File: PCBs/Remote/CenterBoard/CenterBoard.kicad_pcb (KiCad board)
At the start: 4 copper layers, 100 x 100 mm, 83 parts, among them J201 DX07S016JA1R1500, J401 SMA, J501 Conn_01x11, J701 Conn_02x10_Odd_Even, U201 LPC51U68JBD64, U202 W25Q128JVS, U301 SC189ZSKTRT, U401 nRF24L01P, U402 RFX2401C, U601 Joystick Left, U602 Joystick Right, U701 74HC14, U702 74HC14, U703 74HC14, X401 16MHz

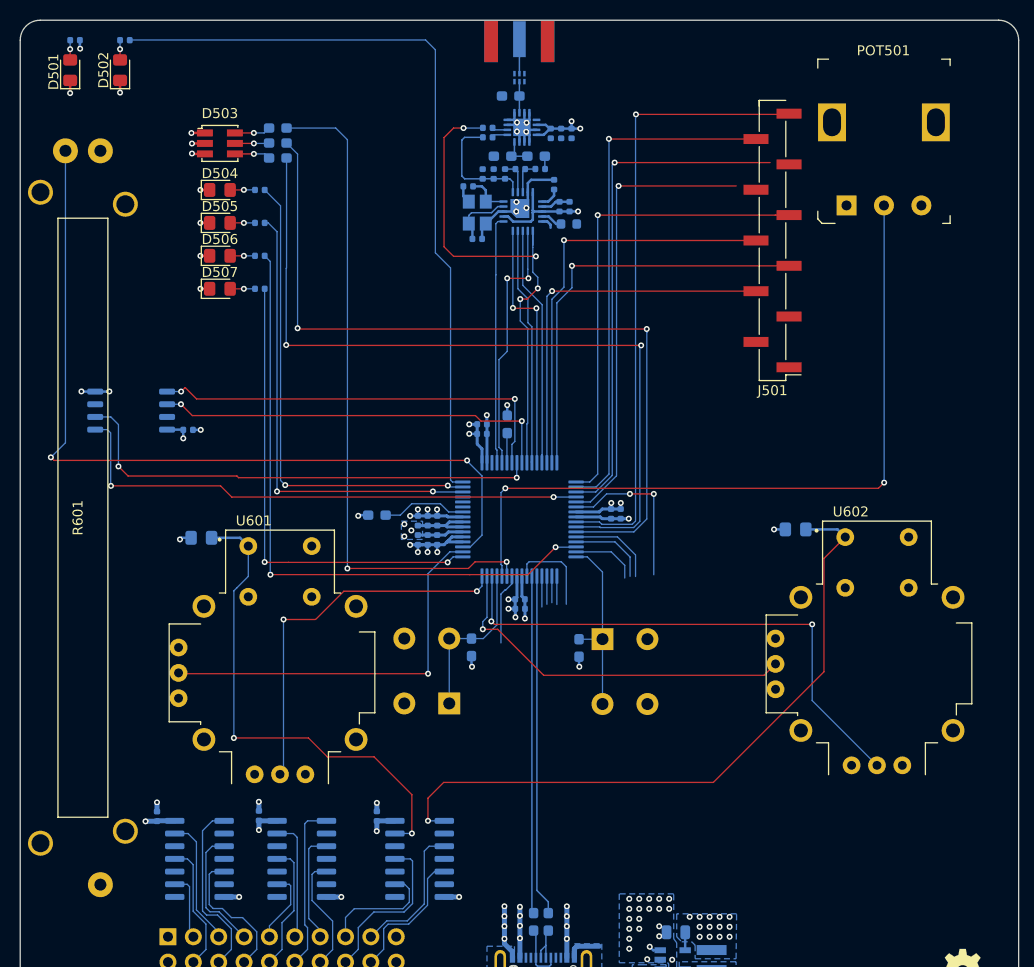
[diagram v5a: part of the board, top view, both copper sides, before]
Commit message: Finished leds, redid a lot of PCB wiring. Almost done there now.
Signed-off-by: Eldalote.Electronics <Eldalote.Electronics@gmail.com>
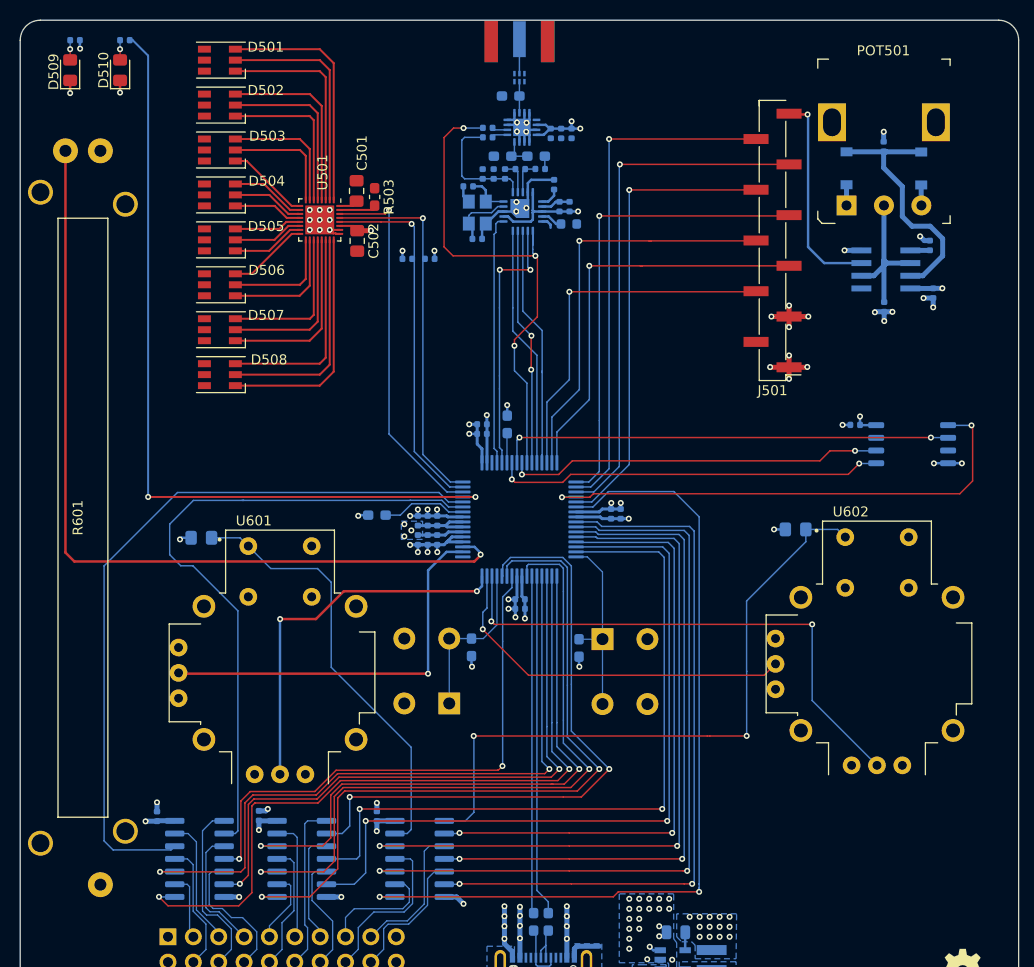
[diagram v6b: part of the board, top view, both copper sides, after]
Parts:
- removed R507, R508, R509: 560R, Resistor_SMD:R_0402_1005Metric
- added C501: 1uF, Capacitor_SMD:C_0805_2012Metric_Pad1.15x1.40mm_HandSolder, F.Cu at (133.7, 77.1)
- added C502: 100nF, Capacitor_SMD:C_0805_2012Metric_Pad1.15x1.40mm_HandSolder, F.Cu at (133.8, 82.1)
- added C503: 100nF, Capacitor_SMD:C_0402_1005Metric, B.Cu at (186.5, 88.7)
- added C504: 100nF, Capacitor_SMD:C_0402_1005Metric, B.Cu at (191.1, 82.6)
- added C505: 100nF, Capacitor_SMD:C_0402_1005Metric, B.Cu at (191.4, 87.3)
- added D501: User LED RGB 0, LED_SMD:LED_RGB_PLCC-6, F.Cu at (120.0, 64.0)
- added D502: User LED RGB 1, LED_SMD:LED_RGB_PLCC-6, F.Cu at (120.0, 68.5)
- added D508: User LED RGB 7, LED_SMD:LED_RGB_PLCC-6, F.Cu at (120.0, 95.5)
- added D511: BAT54GWJ, Diode_SMD:D_SOD-123, B.Cu at (190.2, 74.8)
- added D512: BAT54GWJ, Diode_SMD:D_SOD-123, B.Cu at (182.8, 74.8)
- added U501: LP5024, Package_DFN_QFN:QFN-32-1EP_4x4mm_P0.4mm_EP2.9x2.9mm, F.Cu at (130.0, 80.0)
- added U502: TLC555CDR, digikey-footprints:SOIC-8_W3.9mm, B.Cu at (186.7, 85.0)
- D503: value RGB User LED -> User LED RGB 2; footprint digikey-footprints:6-PLCC_3.5x3.5mm -> LED_SMD:LED_RGB_PLCC-6
- D504: value LED_USER_0 -> User LED RGB 3; footprint LED_SMD:LED_0805_2012Metric_Pad1.15x1.40mm_HandSolder -> LED_SMD:LED_RGB_PLCC-6
- D505: value LED_USER_1 -> User LED RGB 4; footprint LED_SMD:LED_0805_2012Metric_Pad1.15x1.40mm_HandSolder -> LED_SMD:LED_RGB_PLCC-6
- D506: value LED_USER_2 -> User LED RGB 5; footprint LED_SMD:LED_0805_2012Metric_Pad1.15x1.40mm_HandSolder -> LED_SMD:LED_RGB_PLCC-6
- D507: value LED_USER_3 -> User LED RGB 6; footprint LED_SMD:LED_0805_2012Metric_Pad1.15x1.40mm_HandSolder -> LED_SMD:LED_RGB_PLCC-6
- POT501: value Screen brightness Potentiometer -> P120PKY25BR10K
- R503: value 30R -> 7k32; moved to F.Cu
- R504: value 240R -> 1k; footprint Resistor_SMD:R_0603_1608Metric_Pad1.05x0.95mm_HandSolder -> Resistor_SMD:R_0402_1005Metric
- R505: value 240R -> 4k7; footprint Resistor_SMD:R_0603_1608Metric_Pad1.05x0.95mm_HandSolder -> Resistor_SMD:R_0402_1005Metric
- R506: value 560R -> 4k7
- moved U202 78.3 mm to (189.3, 102.5), turned to 180 degrees
- moved C214 66.8 mm to (183.6, 100.5), turned to 180 degrees
- moved R504 60.7 mm to (186.5, 72.7), turned to 90 degrees
- moved R506 18.4 mm to (141.0, 83.9)
- moved R505 16.4 mm to (138.8, 83.9)
- moved R503 11.9 mm to (135.5, 77.7), turned to 270 degrees
- moved D507 4.10 mm to (120.0, 91.0), turned to 180 degrees
- moved D506 2.90 mm to (120.0, 86.5), turned to 180 degrees
- moved D505 1.70 mm to (120.0, 82.0), turned to 180 degrees
- moved D503 0.66 mm to (120.0, 73.0), turned to 180 degrees
- moved D504 0.50 mm to (120.0, 77.5), turned to 180 degrees
- renumbered D501 to D509, D502 to D510
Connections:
- D503 pad 1: GND -> Net-(D503-Pad1)
- D503 pad 2: GND -> Net-(D503-Pad2)
- D503 pad 3: GND -> Net-(D503-Pad3)
- D503 pad 4: Net-(D503-Pad4) -> +3V3
- D503 pad 5: Net-(D503-Pad5) -> +3V3
- D503 pad 6: Net-(D503-Pad6) -> +3V3
- D504 pad 1: GND -> Net-(D504-Pad1)
- D505 pad 1: GND -> Net-(D505-Pad1)
- D506 pad 1: GND -> Net-(D506-Pad1)
- D507 pad 1: GND -> Net-(D507-Pad1)
- J501 pad 11: Screen_Backlight_PWM -> /LEDs and Screen/Backlight_PWM
- POT501 pad 1: GND -> Net-(D512-Pad1)
- POT501 pad 2: Screen_Backlight_pot -> /LEDs and Screen/TRIG
- POT501 pad 3: +3V3 -> Net-(D511-Pad2)
- R503 pad 1: LED_USER_RGB_B -> GND
- R503 pad 2: Net-(D503-Pad6) -> Net-(R503-Pad2)
- R504 pad 1: LED_USER_RGB_G -> /LEDs and Screen/DISCH
- R504 pad 2: Net-(D503-Pad5) -> +3V3
- R505 pad 1: LED_USER_RGB_R -> LED_RGB_I2C_SDA
- R505 pad 2: Net-(D503-Pad4) -> +3V3
- R506 pad 1: Net-(D504-Pad2) -> LED_RGB_I2C_SCL
- R506 pad 2: USER_LED_0 -> +3V3
- U201 pad 1: Net-(U201-Pad1) -> KB_SW_6
- U201 pad 10: Net-(U201-Pad10) -> KB_SW_5
- U201 pad 11: LED_USER_RGB_B -> KB_SW_point
- U201 pad 12: Screen_Backlight_pot -> KB_SW_9
- U201 pad 17: USER_LED_3 -> Net-(U201-Pad17)
- U201 pad 2: Net-(U201-Pad2) -> KB_SW_7
- U201 pad 27: Net-(U201-Pad27) -> KB_SW_0
- U201 pad 28: Net-(U201-Pad28) -> KB_SW_1
- U201 pad 29: Net-(U201-Pad29) -> LED_ERROR
- U201 pad 3: Net-(U201-Pad3) -> KB_SW_8
- U201 pad 30: USER_LED_1 -> LED_RGB_EN
- U201 pad 31: USER_LED_0 -> LED_RGB_I2C_SDA
- U201 pad 32: LED_ERROR -> LED_RGB_I2C_SCL
- U201 pad 4: Net-(U201-Pad4) -> KB_SW_4
- U201 pad 51: Net-(U201-Pad51) -> Screen_TFT_DC
- U201 pad 53: Net-(U201-Pad53) -> Screen_TFT_RESET
- U201 pad 54: Net-(U201-Pad54) -> KB_SW_M3
- U201 pad 57: Screen_Backlight_PWM -> KB_SW_M1
- U201 pad 58: LED_USER_RGB_R -> KB_SW_M0
- U201 pad 59: LED_USER_RGB_G -> KB_SW_M2
- U201 pad 60: Net-(U201-Pad60) -> JS_left_button_out
- U201 pad 61: Net-(U201-Pad61) -> JS_right_button_out
- U201 pad 62: USER_LED_2 -> KB_SW_3
- U201 pad 63: Net-(U201-Pad63) -> KB_SW_ENTER
- U201 pad 7: Net-(U201-Pad7) -> KB_SW_2
- U701 pad 10: Net-(U701-Pad10) -> KB_SW_4
- U701 pad 12: Net-(U701-Pad12) -> KB_SW_1
- U701 pad 2: Net-(U701-Pad2) -> KB_SW_0
- U701 pad 4: Net-(U701-Pad4) -> KB_SW_5
- U701 pad 6: Net-(U701-Pad6) -> KB_SW_8
- U701 pad 8: Net-(U701-Pad8) -> KB_SW_7
- U702 pad 10: Net-(U702-Pad10) -> KB_SW_2
- U702 pad 12: Net-(U702-Pad12) -> KB_SW_6
- U702 pad 2: Net-(U702-Pad2) -> KB_SW_9
- U702 pad 4: Net-(U702-Pad4) -> KB_SW_ENTER
- U702 pad 6: Net-(U702-Pad6) -> KB_SW_3
- U702 pad 8: Net-(U702-Pad8) -> KB_SW_point
- U703 pad 10: Net-(U703-Pad10) -> KB_SW_M0
- U703 pad 12: Net-(U703-Pad12) -> JS_left_button_out
- U703 pad 2: Net-(U703-Pad2) -> JS_right_button_out
- U703 pad 4: Net-(U703-Pad4) -> KB_SW_M2
- U703 pad 6: Net-(U703-Pad6) -> KB_SW_M1
- U703 pad 8: Net-(U703-Pad8) -> KB_SW_M3
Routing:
- net KB_SW_M3: track 0.00 -> 85.4 mm, vias 0 -> 2
- net LED_USER_RGB_G: track 80.7 -> 0.00 mm, vias 2 -> 0
- net LED_USER_RGB_R: track 78.7 -> 0.00 mm, vias 2 -> 0
- net KB_SW_M0: track 0.00 -> 77.7 mm, vias 0 -> 2
- net KB_SW_3: track 0.00 -> 76.3 mm, vias 0 -> 2
- net Screen_Backlight_pot: track 75.0 -> 0.00 mm, vias 2 -> 0
- net KB_SW_1: track 0.00 -> 74.5 mm
- net KB_SW_7: track 0.00 -> 73.9 mm, vias 0 -> 2
- net KB_SW_point: track 0.00 -> 73.9 mm, vias 0 -> 2
- net KB_SW_ENTER: track 0.00 -> 72.8 mm, vias 0 -> 2
- net KB_SW_M1: track 0.00 -> 72.5 mm, vias 0 -> 2
- net JS_left_button_out: track 0.00 -> 72.3 mm, vias 0 -> 2
- net KB_SW_2: track 0.00 -> 68.7 mm, vias 0 -> 2
- net KB_SW_4: track 0.00 -> 68.2 mm, vias 0 -> 2
- net LED_USER_RGB_B: track 67.2 -> 0.00 mm, vias 2 -> 0
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
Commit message: Centerboard v0.1 is done.
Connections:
- U502 pad 1: Net-(U502-Pad1) -> GND
- U601 pad S1: Net-(U601-PadS1) -> GND
- U601 pad S2: Net-(U601-PadS1) -> GND
- U601 pad S3: Net-(U601-PadS1) -> GND
- U601 pad S4: Net-(U601-PadS1) -> GND
- U602 pad S1: Net-(U602-PadS1) -> GND
- U602 pad S2: Net-(U602-PadS1) -> GND
- U602 pad S3: Net-(U602-PadS1) -> GND
- U602 pad S4: Net-(U602-PadS1) -> GND
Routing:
- net +3V3: track 80.3 -> 182.8 mm, vias 43 -> 61
- net +5V: track 11.4 -> 22.9 mm
- net Net-(POT501-Pad4): track 0.00 -> 10.4 mm
- net GND: track 106.0 -> 108.8 mm, vias 90 -> 153
- added copper zone on F.Cu, net GND

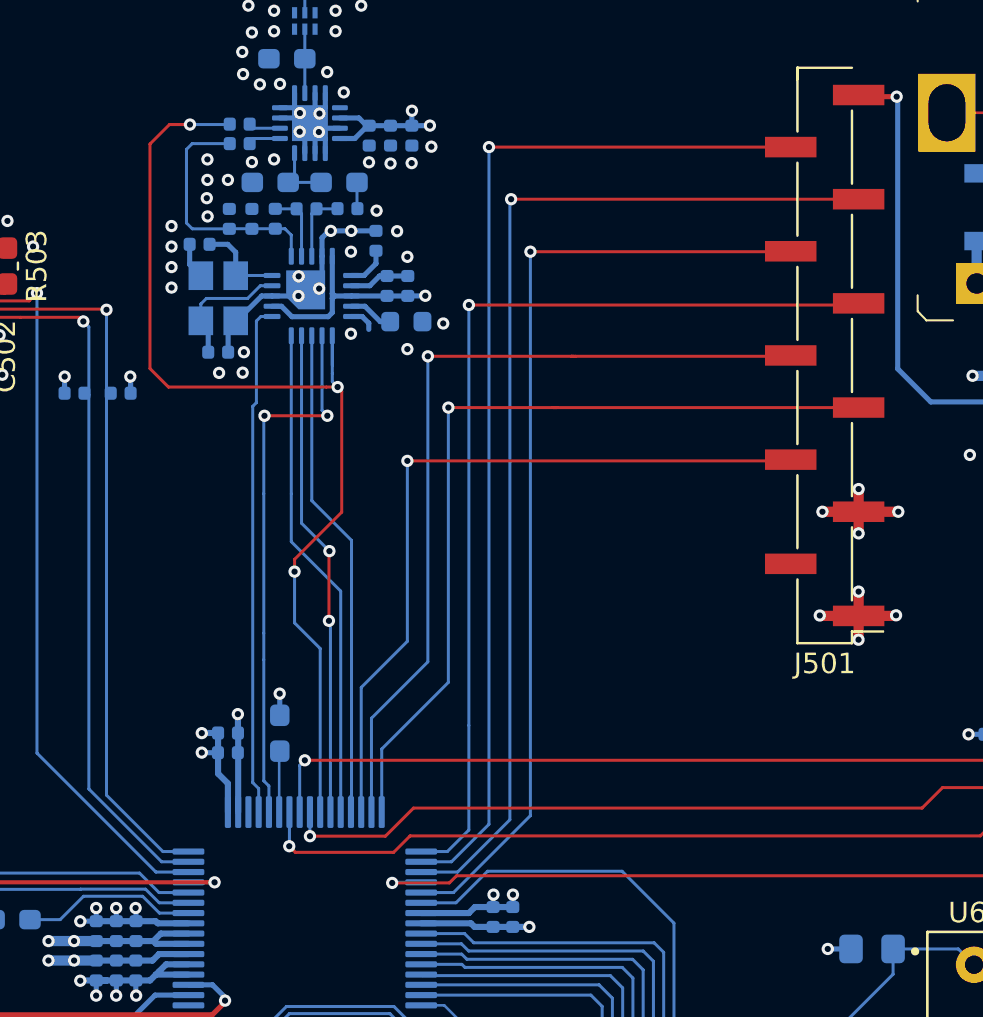
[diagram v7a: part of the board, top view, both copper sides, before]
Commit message: Redid the radio PCB layout on both drone and remote PCB. Drone PCB had old schematic, remote PCB layout wasn't ideal.
Copied in the VHDL project files from the seperate VHDL project into the main "All in one" project.

Signed-off-by: Eldalote.Electronics <Eldalote.Electronics@gmail.com>
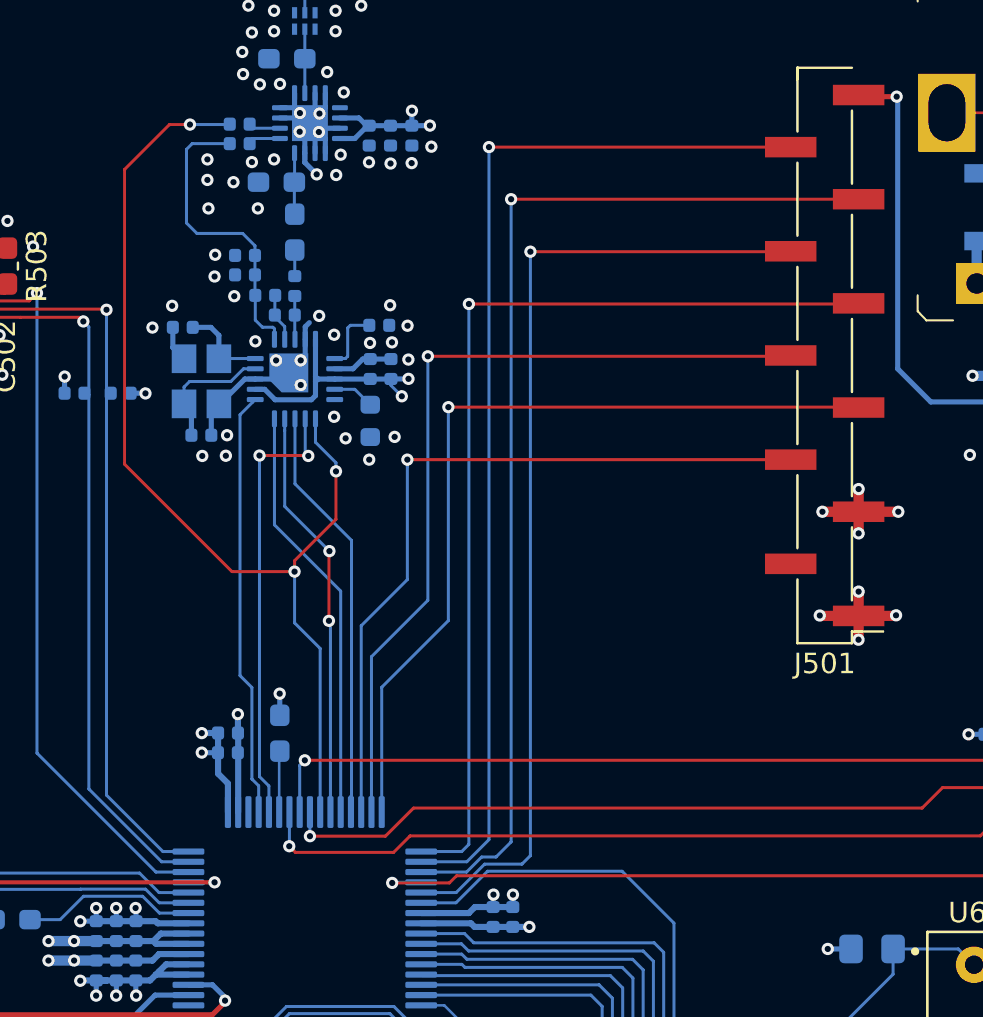
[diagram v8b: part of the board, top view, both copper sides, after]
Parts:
- moved L401 5.29 mm to (149.0, 80.1)
- moved C401 5.15 mm to (153.2, 85.2), turned to 270 degrees
- moved L403 4.57 mm to (149.5, 78.7), turned to 90 degrees
- moved C403 4.13 mm to (154.2, 82.7)
- moved C402 4.13 mm to (153.2, 82.7)
- moved C404 4.13 mm to (145.0, 86.0)
- moved C405 4.13 mm to (144.1, 80.7)
- moved U401 4.13 mm to (149.5, 83.2)
- moved X401 4.13 mm to (145.0, 83.3)
- moved R401 4.12 mm to (153.6, 80.6), turned to 0 degrees
- moved L402 3.77 mm to (148.1, 79.1), turned to 180 degrees
- moved C407 3.25 mm to (149.5, 76.0), turned to 270 degrees
- moved C409 2.75 mm to (147.1, 78.1), turned to 0 degrees
- moved C406 1.94 mm to (147.1, 77.2), turned to 0 degrees
- moved C408 0.30 mm to (148.6, 73.6)
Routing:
- net nRF_CSn: track 26.5 -> 21.8 mm
- net nRF_IRQ: track 25.0 -> 20.8 mm
- net nRF_SCLK: track 24.2 -> 20.5 mm
- net nRF_MISO: track 24.2 -> 20.5 mm
- net nRF_MOSI: track 23.8 -> 20.1 mm
- net GND: track 108.8 -> 106.0 mm, vias 153 -> 160
- net /Radio/VDD_PA: track 12.2 -> 14.9 mm
- net Net-(L401-Pad2): track 3.44 -> 2.12 mm
- net Screen_TFT_RESET: track 47.1 -> 48.2 mm
- net Net-(R401-Pad1): track 2.06 -> 3.17 mm
- net Net-(L401-Pad1): track 3.45 -> 2.35 mm
- net +3V3: track 182.8 -> 183.8 mm, vias 61 -> 62
- net nRF_CE: track 51.1 -> 51.8 mm
- net Screen_TFT_DC: track 52.6 -> 53.3 mm
